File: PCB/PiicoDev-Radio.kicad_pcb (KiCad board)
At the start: 2 copper layers, 25.4 x 52 mm, 22 parts, among them J1 , J2 , J3 Conn_01x05_Male, SW1 ADDR, U1 ATtiny1616-M

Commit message: Update
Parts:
- added C2: 100n, Capacitor_SMD:C_0402_1005Metric, F.Cu at (79.1, 77.7)
- added J4: Conn_Coaxial, Connector_Coaxial:SMB_Jack_Vertical, F.Cu at (97.3, 66.9)
- added U2: RFM69HCW, RF_Module:HOPERF_RFM9XW_SMD, F.Cu at (97.3, 79.5)
- moved G1 25.8 mm to (97.3, 90.3)
- moved G2 15.1 mm to (87.9, 90.5)
- moved C1 10.0 mm to (100.2, 100.5)
- moved G3 10.0 mm to (97.3, 74.5)
- moved R4 10.0 mm to (93.9, 100.6)
- moved SW1 10.0 mm to (97.3, 109.5)
- moved U1 10.0 mm to (97.3, 100.6)
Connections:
- U1 pad 8: Net-(RV1-Pad2) -> unconnected-(U1-Pad8)
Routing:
- net /RF: track 0.00 -> 11.2 mm
- net /UPDI: track 21.0 -> 18.5 mm
- net GND: track 14.9 -> 12.9 mm, vias 7 -> 17
- added copper zone on F.Cu, net GND

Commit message: Basic design complete
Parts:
- added C3: 100u, Capacitor_SMD:C_0603_1608Metric, F.Cu at (97.3, 88.6)
- added D2: LED, LED_SMD:LED_0603_1608Metric, F.Cu at (103.6, 68.2)
- added JP1: SolderJumper_2_Bridged, CoreElectronics_Components:SolderJumper-2_P1.3mm_Bridged_RoundedPad1.0x1.5mm, B.Cu at (108.2, 75.7)
- added R5: 510R, Resistor_SMD:R_0402_1005Metric, F.Cu at (108.2, 71.6)
- JP2: moved to B.Cu
- moved G2 19.2 mm to (106.9, 93.0)
- moved C2 9.13 mm to (87.6, 81.0), turned to 90 degrees
- moved G3 7.89 mm to (97.2, 82.4)
- moved LOGO1 3.63 mm to (103.3, 107.4)
- moved FID1 1.16 mm to (91.6, 112.6)
- moved G1 1.09 mm to (97.3, 91.4)
- moved R4 0.74 mm to (93.9, 101.4)
- moved U1 0.74 mm to (97.3, 101.4)
- moved SW1 0.68 mm to (97.3, 110.2)
- moved FID2 0.49 mm to (108.5, 69.0)
- moved C1 0.32 mm to (100.0, 100.7)
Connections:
- U1 pad 1: unconnected-(U1-Pad1) -> /MISO
- U1 pad 10: unconnected-(U1-Pad10) -> /DIO0
- U1 pad 11: unconnected-(U1-Pad11) -> /DIO4
- U1 pad 12: unconnected-(U1-Pad12) -> /DIO3
- U1 pad 15: unconnected-(U1-Pad15) -> /ADD4
- U1 pad 16: /ADD4 -> /ADD3
- U1 pad 17: /ADD3 -> /ADD2
- U1 pad 18: /ADD2 -> /ADD1
- U1 pad 2: /PWR_LED -> /SCK
- U1 pad 20: /ADD1 -> /MOSI
- U1 pad 5: unconnected-(U1-Pad5) -> /NSS
- U1 pad 6: unconnected-(U1-Pad6) -> /PWR_LED
- U1 pad 7: unconnected-(U1-Pad7) -> /RESET
- U1 pad 8: unconnected-(U1-Pad8) -> /DIO2
- U1 pad 9: unconnected-(U1-Pad9) -> /DIO1
- U2 pad 11: unconnected-(U2-Pad11) -> /DIO3
- U2 pad 12: unconnected-(U2-Pad12) -> /DIO4
- U2 pad 13: unconnected-(U2-Pad13) -> +3V3
- U2 pad 14: unconnected-(U2-Pad14) -> /DIO0
- U2 pad 15: unconnected-(U2-Pad15) -> /DIO1
- U2 pad 16: unconnected-(U2-Pad16) -> /DIO2
- U2 pad 2: unconnected-(U2-Pad2) -> /MISO
- U2 pad 3: unconnected-(U2-Pad3) -> /MOSI
- U2 pad 4: unconnected-(U2-Pad4) -> /SCK
- U2 pad 5: unconnected-(U2-Pad5) -> /NSS
- U2 pad 6: unconnected-(U2-Pad6) -> /RESET
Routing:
- net /DIO0: track 0.00 -> 55.3 mm, vias 0 -> 5
- net /RESET: track 0.00 -> 30.9 mm, vias 0 -> 2
- net /DIO3: track 0.00 -> 30.1 mm
- net /SCK: track 0.00 -> 30.0 mm, vias 0 -> 2
- net /NSS: track 0.00 -> 29.1 mm, vias 0 -> 2
- net /DIO4: track 0.00 -> 27.9 mm
- net /MOSI: track 0.00 -> 27.0 mm
- net +3V3: track 45.0 -> 72.0 mm
- net /MISO: track 0.00 -> 23.5 mm
- net /DIO1: track 0.00 -> 20.7 mm
- net /DIO2: track 0.00 -> 16.7 mm
- net /SCL: track 44.8 -> 29.3 mm, vias 4 -> 3
- net /PWR_LED: track 26.1 -> 13.7 mm, vias 0 -> 2
- net /SDA: track 44.2 -> 37.1 mm
- net GND: track 12.9 -> 19.5 mm, vias 17 -> 22
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- removed copper zone on F.Cu, net (none)
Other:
- board text added: "TX/RX"
- board text added: "TX/RX LED"

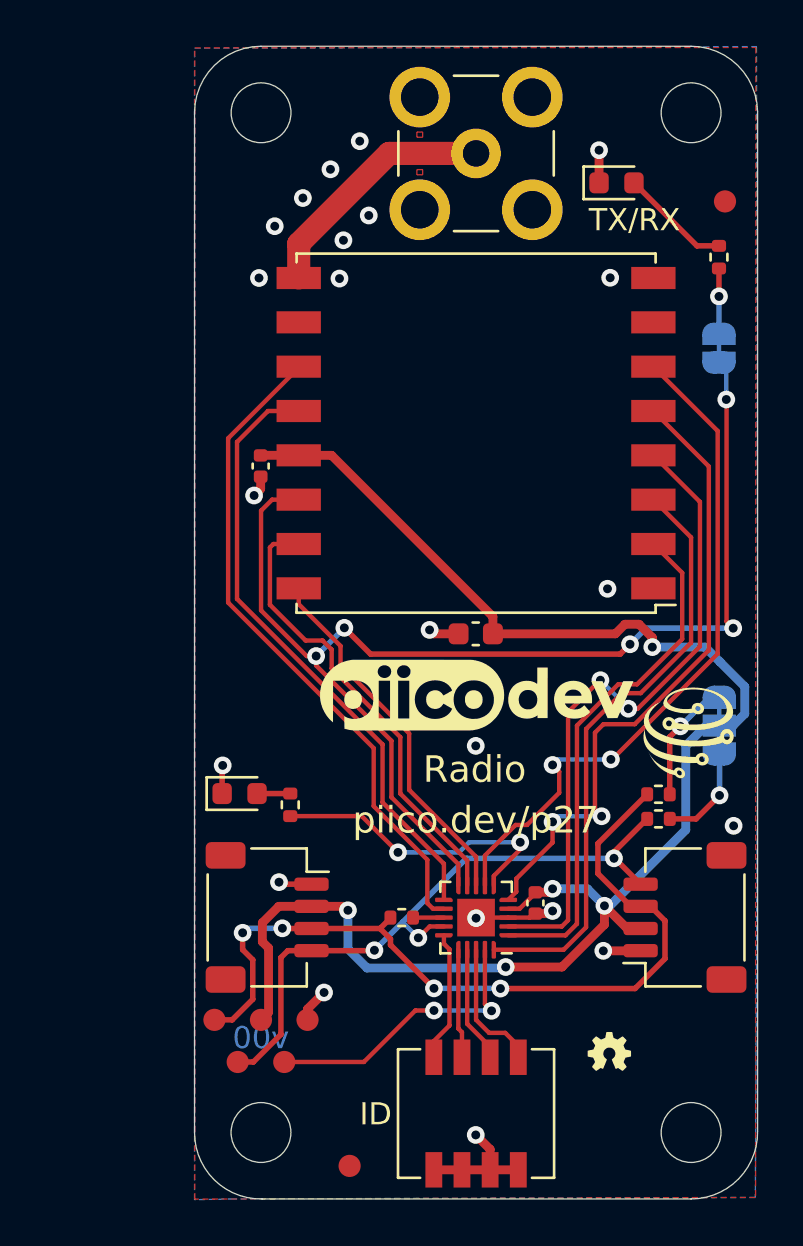
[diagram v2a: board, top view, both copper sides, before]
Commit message: Add jumpers to allow external pull-up resistors
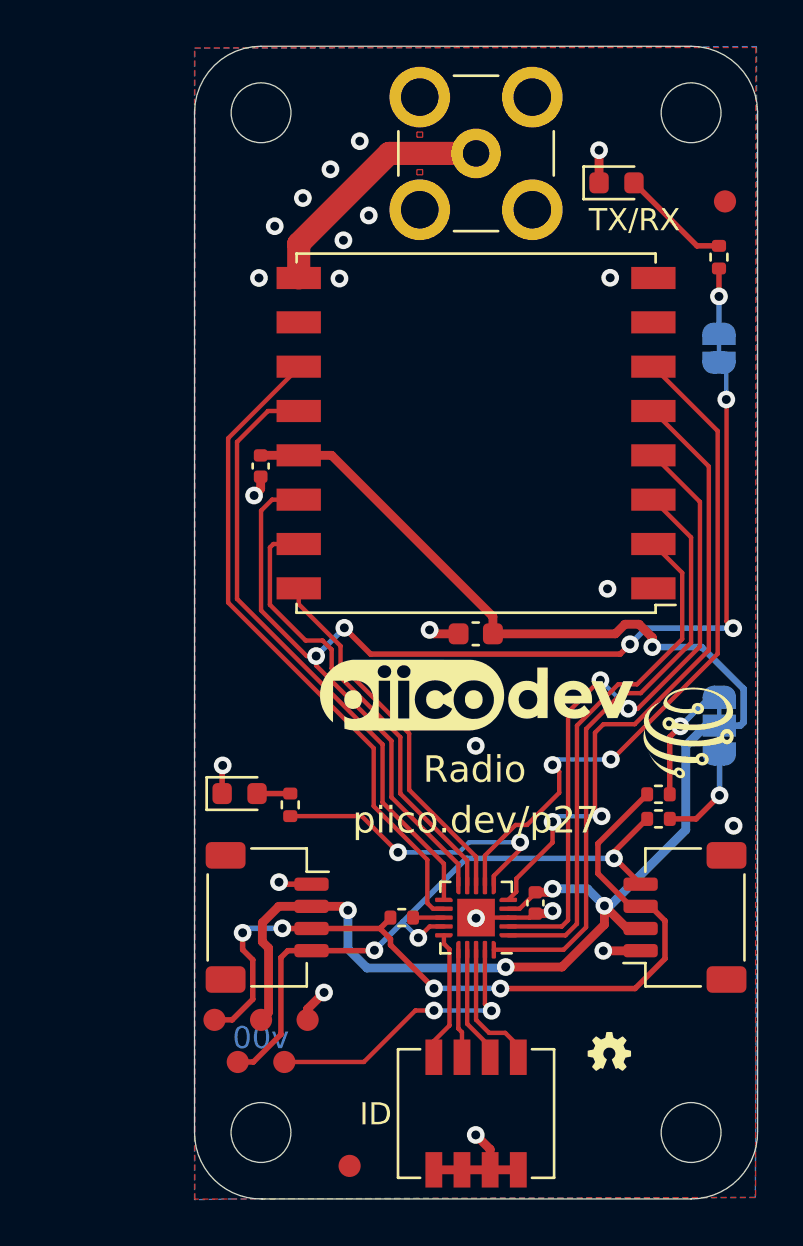
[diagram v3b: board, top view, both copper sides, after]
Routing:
- net +3V3: track 72.0 -> 72.7 mm
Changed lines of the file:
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@@
       (drillshape 0)
       (scaleselection 1)
-      (outputdirectory "gerbers/")
+      (outputdirectory "gerbers")
     )
   )
@@
   (net 25 "/DIO0")
   (net 26 "unconnected-(U2-Pad7)")
-  (net 27 "Net-(R5-Pad2)")
-  (net 28 "Net-(R5-Pad1)")
+  (net 27 "Net-(D2-Pad2)")
+  (net 28 "Net-(JP1-Pad1)")
   (footprint "Connector_JST:JST_SH_SM04B-SRSS-TB_1x04-1MP_P1.00mm_Horizontal" locked (layer "F.Cu")
     (at 106.7054 101.346 90)
@@
     (fp_line (start -0.525 -0.27) (end 0.525 -0.27) (layer "F.Fab") (width 0.1))
     (pad "1" smd roundrect (at -0.51 0 90) (size 0.54 0.64) (layers "F.Cu" "F.Paste" "F.Mask") (roundrect_rratio 0.25)
-      (net 28 "Net-(R5-Pad1)") (pintype "passive"))
+      (net 28 "Net-(JP1-Pad1)") (pintype "passive"))
     (pad "2" smd roundrect (at 0.51 0 90) (size 0.54 0.64) (layers "F.Cu" "F.Paste" "F.Mask") (roundrect_rratio 0.25)
-      (net 27 "Net-(R5-Pad2)") (pintype "passive"))
+      (net 27 "Net-(D2-Pad2)") (pintype "passive"))
     (model "${KICAD6_3DMODEL_DIR}/Resistor_SMD.3dshapes/R_0402_1005Metric.wrl"
       (offset (xyz 0 0 0))
@@
       (net 2 "GND") (pinfunction "K") (pintype "passive"))
     (pad "2" smd roundrect (at 0.7875 0) (size 0.875 0.95) (layers "F.Cu" "F.Paste" "F.Mask") (roundrect_rratio 0.25)
-      (net 27 "Net-(R5-Pad2)") (pinfunction "A") (pintype "passive"))
+      (net 27 "Net-(D2-Pad2)") (pinfunction "A") (pintype "passive"))
     (model "${KICAD6_3DMODEL_DIR}/LED_SMD.3dshapes/LED_0603_1608Metric.wrl"
       (offset (xyz 0 0 0))
@@
   )
   (footprint "CoreElectronics_Components:TestPoint_Pad_D1.0mm_x05_Pattern1" (layer "F.Cu")
-    (at 87.5792 106.9168 -90)
+    (at 87.5822 106.9168 -90)
     (descr "5x1.0mm Pads Pattern 1")
     (tags "testpoint test point pad")
@@
     (fp_line (start -1.65 1.25) (end 1.65 1.25) (layer "B.CrtYd") (width 0.05))
     (pad "1" smd custom locked (at -0.65 0 270) (size 1 0.5) (layers "B.Cu" "B.Mask")
-      (net 28 "Net-(R5-Pad1)") (pinfunction "A") (pintype "passive") (zone_connect 2)
+      (net 28 "Net-(JP1-Pad1)") (pinfunction "A") (pintype "passive") (zone_connect 2)
       (options (clearance outline) (anchor rect))
       (primitives
@@
   (via (at 100.7337 100.054597) (size 0.8) (drill 0.4) (layers "F.Cu" "B.Cu") (net 1))
   (via (at 105.232546 89.150946) (size 0.8) (drill 0.4) (layers "F.Cu" "B.Cu") (net 1))
+  (segment (start 107.465028 89.150946) (end 109.3548 91.040718) (width 0.3) (layer "B.Cu") (net 1))
+  (segment (start 105.232546 89.150946) (end 107.465028 89.150946) (width 0.3) (layer "B.Cu") (net 1))
   (segment (start 91.5018 102.763271) (end 91.5018 101.0234) (width 0.4) (layer "B.Cu") (net 1))
   (segment (start 106.7441 97.396651) (end 103.319951 100.8208) (width 0.4) (layer "B.Cu") (net 1))
-  (segment (start 109.4048 90.9356) (end 109.4048 92.1628) (width 0.4) (layer "B.Cu") (net 1))
-  (segment (start 105.232546 89.150946) (end 107.620146 89.150946) (width 0.4) (layer "B.Cu") (net 1))
-  (segment (start 109.4048 92.1628) (end 108.8748 92.6928) (width 0.4) (layer "B.Cu") (net 1))
+  (segment (start 109.3548 92.543) (end 109.205 92.6928) (width 0.3) (layer "B.Cu") (net 1))
+  (segment (start 109.3548 91.040718) (end 109.3548 92.543) (width 0.3) (layer "B.Cu") (net 1))
   (segment (start 103.319951 100.8208) (end 103.0732 100.8208) (width 0.4) (layer "B.Cu") (net 1))
   (segment (start 103.0732 100.8208) (end 102.306997 100.054597) (width 0.4) (layer "B.Cu") (net 1))
-  (segment (start 107.620146 89.150946) (end 108.2912 89.822) (width 0.4) (layer "B.Cu") (net 1))
-  (segment (start 108.2912 89.822) (end 109.4048 90.9356) (width 0.4) (layer "B.Cu") (net 1))
   (segment (start 108.8748 92.6928) (end 108.2548 92.6928) (width 0.4) (layer "B.Cu") (net 1))
   (segment (start 102.306997 100.054597) (end 100.7337 100.054597) (width 0.4) (layer "B.Cu") (net 1))
+  (segment (start 109.205 92.6928) (end 108.2548 92.6928) (width 0.3) (layer "B.Cu") (net 1))
   (segment (start 106.7441 93.6066) (end 107.6579 92.6928) (width 0.4) (layer "B.Cu") (net 1))
   (segment (start 106.7441 93.6066) (end 106.7441 97.396651) (width 0.4) (layer "B.Cu") (net 1))

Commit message: Remove SMA and add PCB antenna
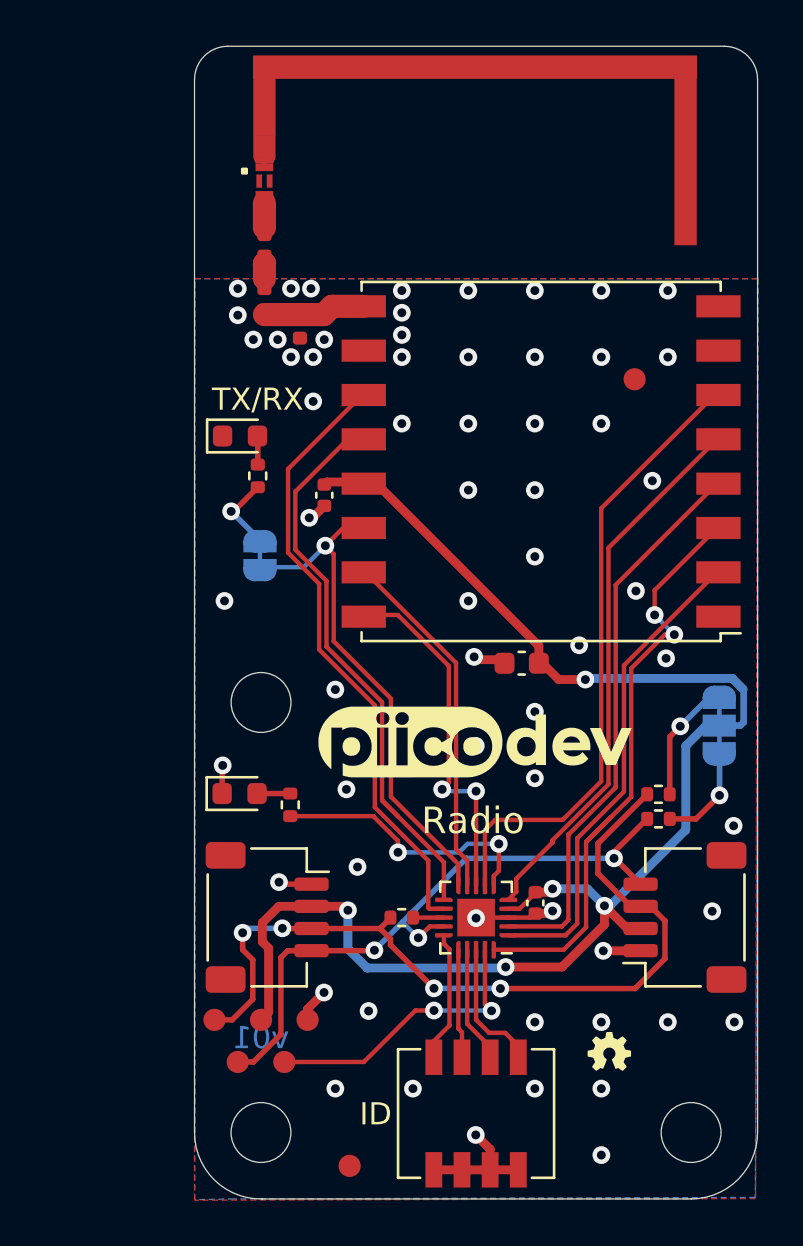
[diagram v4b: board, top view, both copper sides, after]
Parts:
- removed H4: MountingHole, CoreElectronics_Components:MountingHole_2.7mm_M2.5_PadClearance_1.2
- removed J4: Conn_Coaxial, Connector_Coaxial:SMB_Jack_Vertical
- added AE1: Antenna_Chip_No_Antenna_Symbol, CoreElectronics_Components:Antenna_Chip_TDK_ANT160920ST-1204A1, F.Cu at (87.7, 68.1)
- added AE2: Antenna, Project Library:PiicoDev_Radio_Antenna, F.Cu at (87.7, 68.1)
- added L1: L, Inductor_SMD:L_0402_1005Metric, F.Cu at (89.3, 74.7)
- added L2: L, Inductor_SMD:L_0402_1005Metric, F.Cu at (87.7, 73.5)
- added L3: L, Inductor_SMD:L_0402_1005Metric, F.Cu at (87.7, 71.0)
- C3: value 100u -> 10u
- G2: moved to B.Cu
- moved H1 46.0 mm to (87.6, 111.0)
- moved H2 46.0 mm to (107.0, 111.0)
- moved R5 23.0 mm to (87.4, 81.4)
- moved JP1 22.7 mm to (87.5, 85.0)
- moved D2 20.5 mm to (86.6, 79.6)
- moved H3 19.4 mm to (87.6, 91.6)
- moved G2 9.60 mm to (97.3, 92.7), turned to 180 degrees
- moved FID2 9.00 mm to (104.4, 77.1)
- moved U2 3.20 mm to (100.2, 80.8)
- moved C2 3.16 mm to (90.4, 82.3)
- moved G3 3.06 mm to (97.1, 79.4)
- moved C3 2.46 mm to (99.3, 89.9)
- moved G1 2.12 mm to (97.3, 93.5)
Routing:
- net /DIO0: track 55.3 -> 23.8 mm, vias 5 -> 1
- net /RF: track 11.2 -> 4.64 mm
- net /DIO1: track 20.7 -> 16.1 mm
- net /SCK: track 30.0 -> 25.4 mm, vias 2 -> 0
- net /NSS: track 29.1 -> 24.8 mm, vias 2 -> 0
- net +3V3: track 72.7 -> 68.6 mm
- net Net-(D2-Pad2): track 5.01 -> 1.30 mm
- net /RESET: track 30.9 -> 28.3 mm, vias 2 -> 0
- net /DIO3: track 30.1 -> 28.0 mm
- net /DIO4: track 27.9 -> 26.3 mm
- net /MISO: track 23.5 -> 21.9 mm
- net GND: track 19.5 -> 18.0 mm, vias 22 -> 62
- net /PWR_LED: track 13.7 -> 12.5 mm
- net /RF2: track 0.00 -> 1.12 mm
- net Net-(AE2-Pad1): track 0.00 -> 0.92 mm
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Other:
- outline, holes or cut-outs redrawn
- board text added: "v01"
- board text removed: "v00"
